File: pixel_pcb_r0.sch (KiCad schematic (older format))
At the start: 0 parts

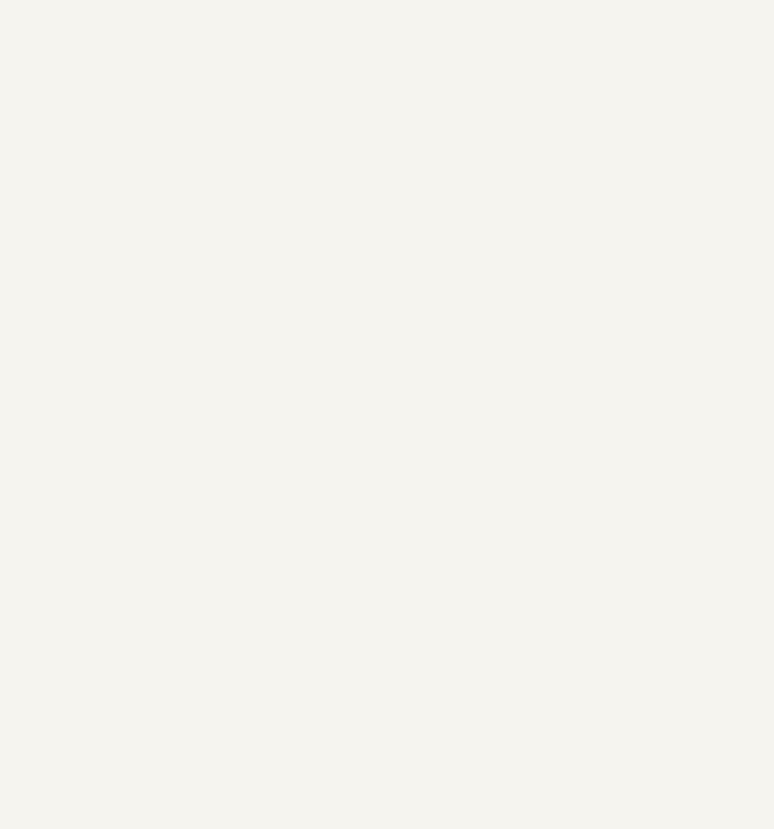
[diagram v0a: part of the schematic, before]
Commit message: k20 symbol added
created parts library and added k20 schematic to it.
uc hierarchical page now located on main page of schematic.
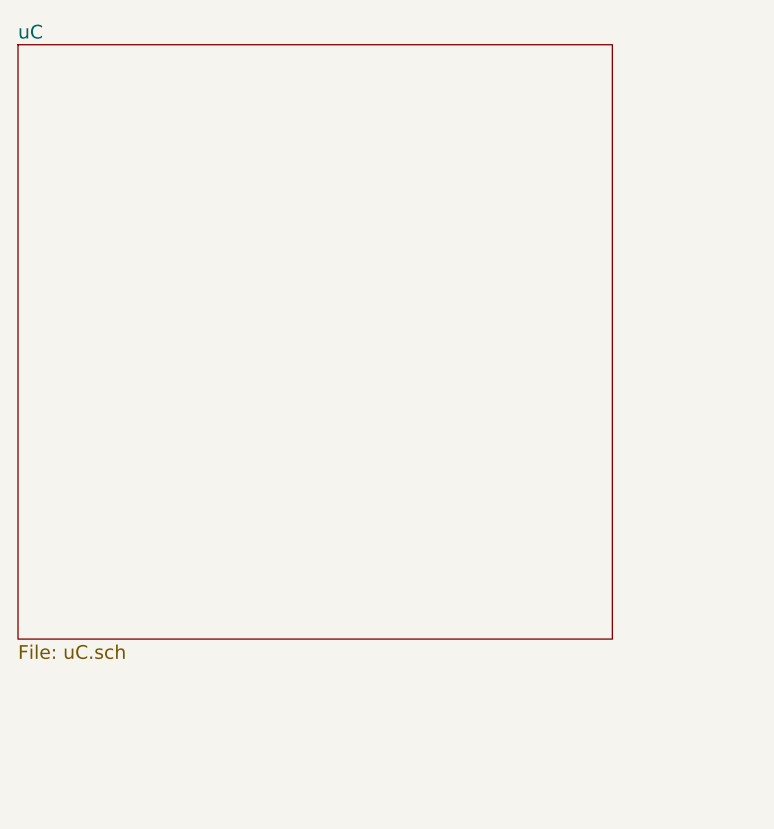
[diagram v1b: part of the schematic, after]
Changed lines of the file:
@@
 LIBS:contrib
 LIBS:valves
+LIBS:pixel_pcb_r0
+LIBS:pixel_pcb_r0-cache
 EELAYER 25 0
 EELAYER END
 $Descr D 34000 22000
 encoding utf-8
-Sheet 1 1
+Sheet 1 2
 Title ""
 Date ""
@@
 Text Notes 32900 21350 0    60   ~ 0
 0
+$Sheet
+S 20500 4750 2600 2600
+U 551787C3
+F0 "uC" 60
+F1 "uC.sch" 60
+$EndSheet
 $EndSCHEMATC
